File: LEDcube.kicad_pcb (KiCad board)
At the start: 2 copper layers, 40 x 40 mm, 29 parts, among them J101 IN, J102 OUT, J103 JTAG, U101 AP1117-33, U102 STM32F030F4Px, U103 SP3485CN, Y101 16MHz

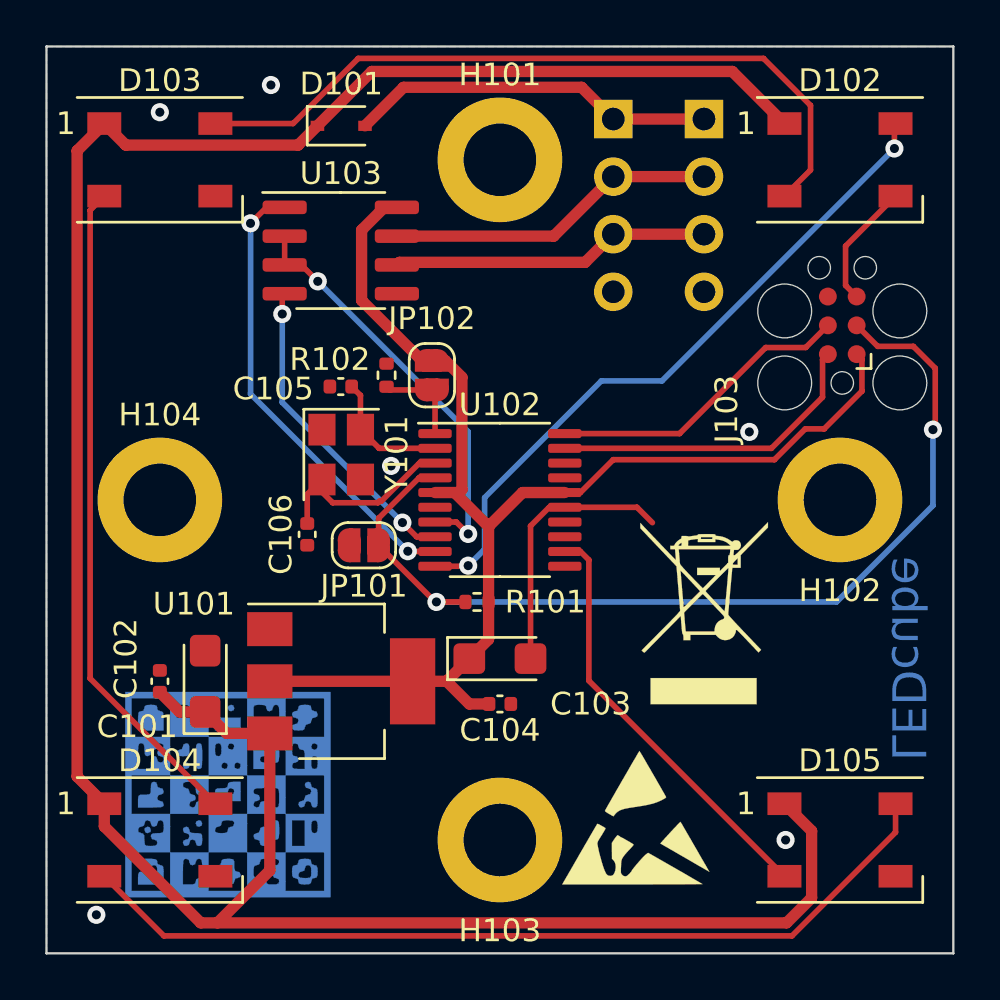
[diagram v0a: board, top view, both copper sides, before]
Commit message: Crystal related fixes
Signed-off-by: Benedikt Spranger <b.spranger@linutronix.de>
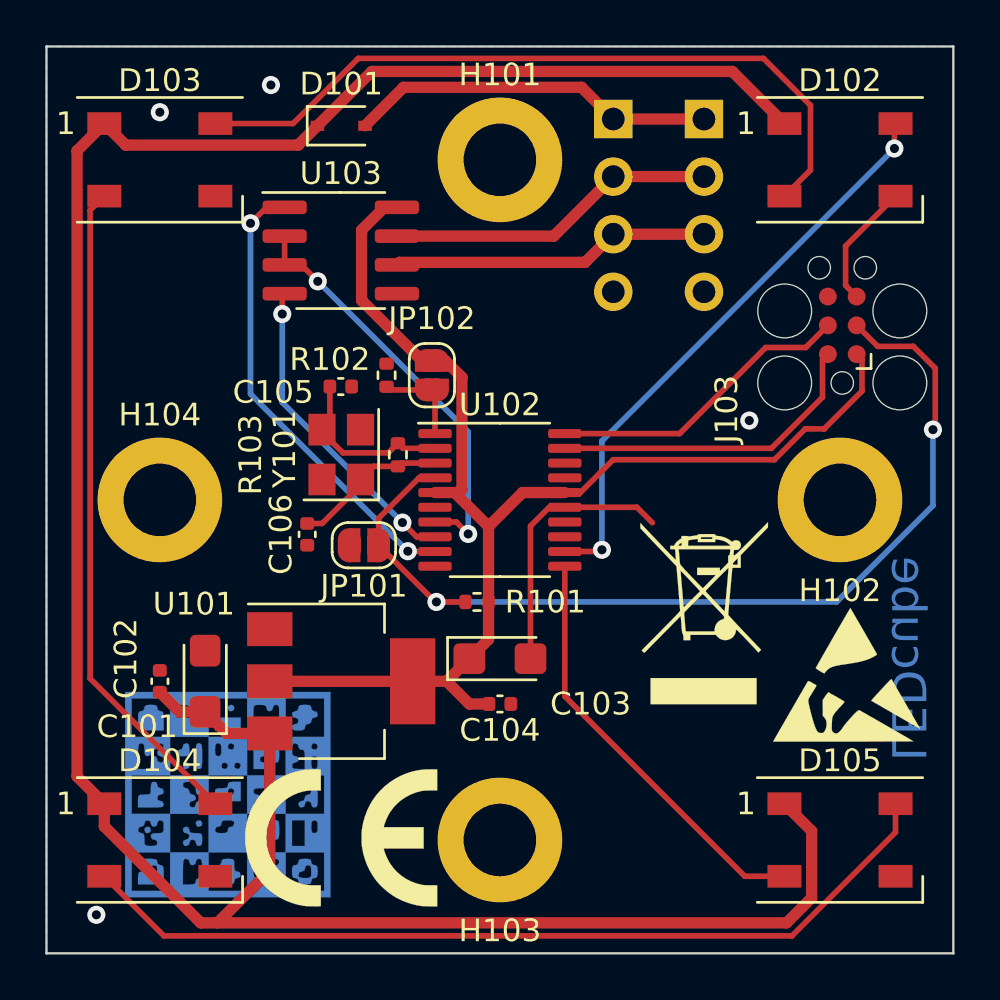
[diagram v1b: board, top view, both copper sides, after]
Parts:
- added R103: 1M, Resistor_SMD:R_0402_1005Metric, F.Cu at (95.5, 98.0)
- added SYM4: CE-Logo_8.5x6mm_SilkScreen, Symbol:CE-Logo_8.5x6mm_SilkScreen, F.Cu at (93.0, 114.9)
- moved SYM3 11.2 mm to (115.3, 107.7)
- turned C105 to 180 degrees
- turned Y101 to 90 degrees
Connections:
- U102 pad 10: /DIN -> unconnected-(U102-Pad10)
- U102 pad 11: unconnected-(U102-Pad11) -> /DOUT
- U102 pad 12: /DOUT -> /DIN
- Y101 pad 1: GND -> Net-(C106-Pad2)
- Y101 pad 2: Net-(C106-Pad2) -> GND
- Y101 pad 3: GND -> Net-(C105-Pad2)
- Y101 pad 4: Net-(C105-Pad2) -> GND
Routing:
- net /DIN: track 30.3 -> 25.8 mm
- net Net-(C105-Pad2): track 5.69 -> 7.78 mm
- net Net-(C106-Pad2): track 8.67 -> 6.89 mm
- net GND: track 17.4 -> 18.0 mm, vias 6 -> 4
